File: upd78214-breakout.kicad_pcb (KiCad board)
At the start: 2 copper layers, 50 x 50 mm, 9 parts, among them U1 upd78214-64p-qfp, U2 tmp87c800df, X1 USB-B1HSB6

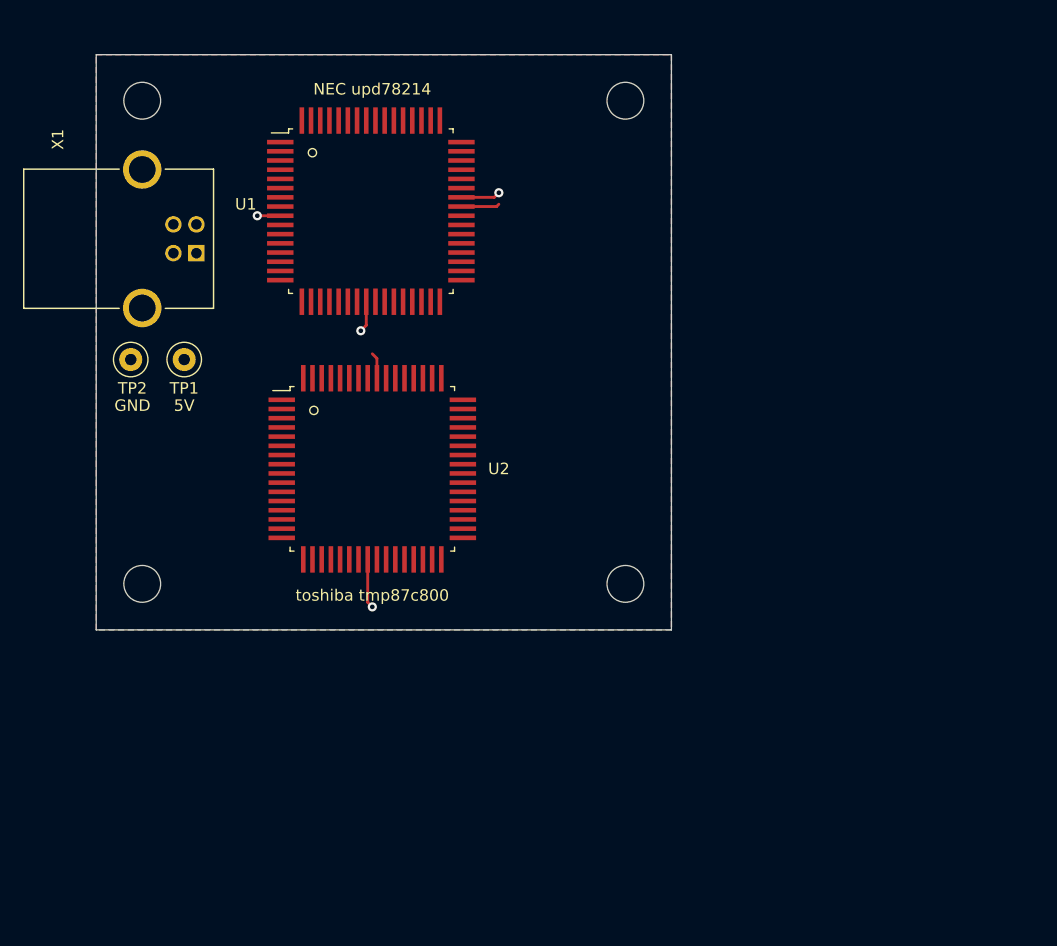
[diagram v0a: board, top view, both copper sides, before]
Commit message: Breakout pins for NEC
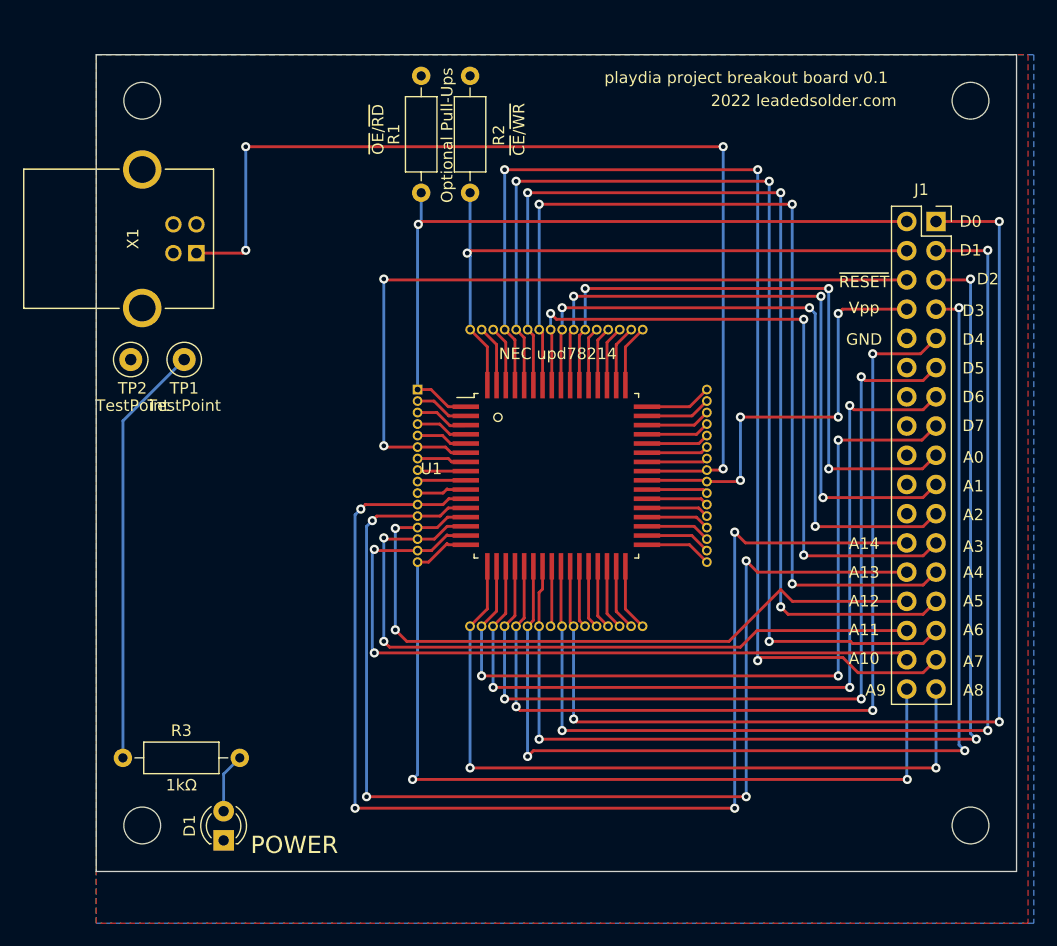
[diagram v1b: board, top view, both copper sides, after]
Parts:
- removed U2: tmp87c800df, NEC:QFP-64_14x14_Pitch0.8mm
- added D1: LED, LED_THT:LED_D3.0mm, F.Cu at (91.1, 147.3)
- added J1: Conn_02x17_Odd_Even, Connector_PinSocket_2.54mm:PinSocket_2x17_P2.54mm_Vertical, F.Cu at (153.0, 93.5)
- added R1: R_Small_US, Resistor_THT:R_Axial_DIN0207_L6.3mm_D2.5mm_P10.16mm_Horizontal, F.Cu at (108.2, 91.0)
- added R2: R_Small_US, Resistor_THT:R_Axial_DIN0207_L6.3mm_D2.5mm_P10.16mm_Horizontal, F.Cu at (112.5, 91.0)
- added R3: 1kΩ, Resistor_THT:R_Axial_DIN0207_L6.3mm_D2.5mm_P10.16mm_Horizontal, F.Cu at (82.3, 140.1)
- TP1: value 5V -> TestPoint
- TP2: value GND -> TestPoint
- moved REF** 69.8 mm to (156.0, 146.0)
- moved REF** 51.6 mm to (156.0, 83.0)
- moved U1 28.1 mm to (120.0, 115.6)
- moved REF** 21.0 mm to (84.0, 146.0)
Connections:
- U1 pad 1: unconnected-(U1-Pad1) -> /~{PROG_OE}
- U1 pad 11: unconnected-(U1-Pad11) -> /PROG_A14
- U1 pad 12: unconnected-(U1-Pad12) -> /PROG_A13
- U1 pad 13: unconnected-(U1-Pad13) -> /PROG_A12
- U1 pad 14: unconnected-(U1-Pad14) -> /PROG_A11
- U1 pad 15: unconnected-(U1-Pad15) -> /PROG_A10
- U1 pad 16: unconnected-(U1-Pad16) -> /PROG_A9
- U1 pad 17: unconnected-(U1-Pad17) -> /PROG_A8
- U1 pad 18: unconnected-(U1-Pad18) -> /PROG_D7
- U1 pad 19: unconnected-(U1-Pad19) -> /PROG_D6
- U1 pad 20: unconnected-(U1-Pad20) -> /PROG_D5
- U1 pad 21: unconnected-(U1-Pad21) -> /PROG_D4
- U1 pad 22: unconnected-(U1-Pad22) -> /PROG_D3
- U1 pad 23: unconnected-(U1-Pad23) -> /PROG_D2
- U1 pad 25: unconnected-(U1-Pad25) -> /PROG_D1
- U1 pad 26: unconnected-(U1-Pad26) -> /PROG_D0
- U1 pad 40: unconnected-(U1-Pad40) -> /PROG_Vpp
- U1 pad 54: unconnected-(U1-Pad54) -> /PROG_A0
- U1 pad 55: unconnected-(U1-Pad55) -> /PROG_A1
- U1 pad 56: unconnected-(U1-Pad56) -> /PROG_A2
- U1 pad 57: unconnected-(U1-Pad57) -> /PROG_A3
- U1 pad 58: unconnected-(U1-Pad58) -> /PROG_A4
- U1 pad 59: unconnected-(U1-Pad59) -> /PROG_A5
- U1 pad 6: unconnected-(U1-Pad6) -> /~{PROG_RESET}
- U1 pad 60: unconnected-(U1-Pad60) -> /PROG_A6
- U1 pad 61: unconnected-(U1-Pad61) -> /PROG_A7
- U1 pad 64: unconnected-(U1-Pad64) -> /~{PROG_CE}
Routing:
- net +5V: track 5.63 -> 126.4 mm, vias 0 -> 4
- net /PROG_A14: track 0.00 -> 108.1 mm, vias 0 -> 4
- net /PROG_A13: track 0.00 -> 100.7 mm, vias 0 -> 4
- net /PROG_A7: track 0.00 -> 100.4 mm, vias 0 -> 3
- net /PROG_D0: track 0.00 -> 99.5 mm, vias 0 -> 3
- net /PROG_D1: track 0.00 -> 97.6 mm, vias 0 -> 3
- net /PROG_D2: track 0.00 -> 96.4 mm, vias 0 -> 3
- net /PROG_D3: track 0.00 -> 95.7 mm, vias 0 -> 3
- net /PROG_A6: track 0.00 -> 95.1 mm, vias 0 -> 3
- net /PROG_A5: track 0.00 -> 89.2 mm, vias 0 -> 3
- net /PROG_A4: track 0.00 -> 83.9 mm, vias 0 -> 3
- net /PROG_D4: track 0.00 -> 80.7 mm, vias 0 -> 3
- net /PROG_D5: track 0.00 -> 78.0 mm, vias 0 -> 3
- net /PROG_A9: track 0.00 -> 74.8 mm, vias 0 -> 2
- net /PROG_D6: track 0.00 -> 74.6 mm, vias 0 -> 3
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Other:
- board size 50 x 50 mm -> 80 x 71 mm
- board text added: "A0"
- board text added: "A1"
- board text added: "A10"
- board text added: "A11"
- board text added: "A12"
- board text added: "A13"
- board text added: "A14"
- board text added: "A2"
- board text added: "A3"
- board text added: "A4"
- board text added: "A5"
- board text added: "A6"
- board text added: "A7"
- board text added: "A8"
- board text added: "A9"
- board text added: "D0"
- board text added: "D1"
- board text added: "D2"
- board text added: "D3"
- board text added: "D4"
- board text added: "D5"
- board text added: "D6"
- board text added: "D7"
- board text added: "GND"
- board text added: "Optional Pull-Ups"
- board text added: "POWER"
- board text added: "Vpp"
- board text added: "~{CE}/~{WR}"
- board text added: "~{OE}/~{RD}"
- board text added: "~{RESET}"
- board text removed: "toshiba tmp87c800"

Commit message: Dumper V1 sent to Jonko
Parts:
- added SPARE: DIP-14_W7.62mm_LongPads, Package_DIP:DIP-14_W7.62mm_LongPads, F.Cu at (88.4, 115.6)
- moved X1 6.81 mm to (90.8, 94.7)
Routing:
- net +5V: track 126.4 -> 71.5 mm, vias 4 -> 2
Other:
- board text added: "+5V"

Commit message: Break out NMI pin
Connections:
- J1 pad 22: unconnected-(J1-Pad22) -> /PROG_NMI
- U1 pad 28: unconnected-(U1-Pad28) -> /PROG_NMI
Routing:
- net /PROG_NMI: track 0.00 -> 51.8 mm, vias 0 -> 3
- net unconnected-(U1-Pad28): track 5.49 -> 0.00 mm
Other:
- board text added: "playdia project breakout board v0.2"
- board text removed: "playdia project breakout board v0.1"
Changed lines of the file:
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@@
   (net 24 "/PROG_A8")
   (net 25 "unconnected-(U1-Pad27)")
-  (net 26 "unconnected-(U1-Pad28)")
+  (net 26 "/PROG_NMI")
   (net 27 "unconnected-(U1-Pad29)")
   (net 28 "unconnected-(U1-Pad30)")
@@
   (net 68 "unconnected-(J1-Pad18)")
   (net 69 "unconnected-(J1-Pad20)")
-  (net 70 "unconnected-(J1-Pad22)")
-  (net 71 "Net-(D1-Pad2)")
+  (net 70 "Net-(D1-Pad2)")
   (footprint "TestPoint:TestPoint_Loop_D2.50mm_Drill1.0mm" (layer "F.Cu")
     (at 83 105.5)
@@
       (net 25 "unconnected-(U1-Pad27)") (pinfunction "ASTB") (pintype "output"))
     (pad "28" smd rect (at 2.8 7.874) (size 0.4 2.3) (layers "F.Cu" "F.Paste" "F.Mask")
-      (net 26 "unconnected-(U1-Pad28)") (pinfunction "p2,0/nmi") (pintype "input"))
+      (net 26 "/PROG_NMI") (pinfunction "p2,0/nmi") (pintype "input"))
     (pad "28" thru_hole oval (at 3.493 13.081 180) (size 0.85 0.85) (drill 0.5) (layers *.Cu *.Mask)
-      (net 26 "unconnected-(U1-Pad28)") (pinfunction "p2,0/nmi") (pintype "input"))
+      (net 26 "/PROG_NMI") (pinfunction "p2,0/nmi") (pintype "input"))
     (pad "29" thru_hole oval (at 4.493 13.081 90) (size 0.85 0.85) (drill 0.5) (layers *.Cu *.Mask)
       (net 27 "unconnected-(U1-Pad29)") (pinfunction "p2,1/intp0") (pintype "input"))
@@
       (net 57 "GND") (pinfunction "K") (pintype "passive"))
     (pad "2" thru_hole circle (at 2.54 0 90) (size 1.8 1.8) (drill 0.9) (layers *.Cu *.Mask)
-      (net 71 "Net-(D1-Pad2)") (pinfunction "A") (pintype "passive"))
+      (net 70 "Net-(D1-Pad2)") (pinfunction "A") (pintype "passive"))
     (model "${KICAD6_3DMODEL_DIR}/LED_THT.3dshapes/LED_D3.0mm.wrl"
       (offset (xyz 0 0 0))
@@
       (net 18 "/PROG_A2") (pinfunction "Pin_21") (pintype "passive"))
     (pad "22" thru_hole oval (at -2.54 25.4) (size 1.7 1.7) (drill 1) (layers *.Cu *.Mask)
-      (net 70 "unconnected-(J1-Pad22)") (pinfunction "Pin_22") (pintype "passive+no_connect"))
+      (net 26 "/PROG_NMI") (pinfunction "Pin_22") (pintype "passive"))
     (pad "23" thru_hole oval (at 0 27.94) (size 1.7 1.7) (drill 1) (layers *.Cu *.Mask)
       (net 19 "/PROG_A3") (pinfunction "Pin_23") (pintype "passive"))
@@
       (net 58 "+5V") (pintype "passive"))
     (pad "2" thru_hole oval (at 10.16 0) (size 1.6 1.6) (drill 0.8) (layers *.Cu *.Mask)
-      (net 71 "Net-(D1-Pad2)") (pintype "passive"))
+      (net 70 "Net-(D1-Pad2)") (pintype "passive"))
     (model "${KICAD6_3DMODEL_DIR}/Resistor_THT.3dshapes/R_Axial_DIN0207_L6.3mm_D2.5mm_P10.16mm_Horizontal.wrl"
       (offset (xyz 0 0 0))
@@
       (effects (font (size 1.001228 1.001228) (thickness 0.15)))
     )
+    (fp_line (start 6.05 2) (end 6.05 10.3) (layer "F.SilkS") (width 0.127))
+    (fp_line (start 6.05 -6.2) (end 6.05 -2) (layer "F.SilkS") (width 0.127))
+    (fp_line (start -6.05 -2) (end -6.05 -6.2) (layer "F.SilkS") (width 0.127))
+    (fp_line (start -6.05 10.3) (end -6.05 2) (layer "F.SilkS") (width 0.127))
     (fp_line (start -6.05 -6.2) (end 6.05 -6.2) (layer "F.SilkS") (width 0.127))
-    (fp_line (start -6.05 -2) (end -6.05 -6.2) (layer "F.SilkS") (width 0.127))
-    (fp_line (start 6.05 -6.2) (end 6.05 -2) (layer "F.SilkS") (width 0.127))
-    (fp_line (start 6.05 2) (end 6.05 10.3) (layer "F.SilkS") (width 0.127))
-    (fp_line (start -6.05 10.3) (end -6.05 2) (layer "F.SilkS") (width 0.127))
     (fp_line (start 6.05 10.3) (end -6.05 10.3) (layer "F.SilkS") (width 0.127))
+    (fp_line (start -8 -6.5) (end 8 -6.5) (layer "F.CrtYd") (width 0.05))
     (fp_line (start 8 10.5) (end -8 10.5) (layer "F.CrtYd") (width 0.05))
+    (fp_line (start 8 -6.5) (end 8 10.5) (layer "F.CrtYd") (width 0.05))
     (fp_line (start -8 10.5) (end -8 -6.5) (layer "F.CrtYd") (width 0.05))
-    (fp_line (start -8 -6.5) (end 8 -6.5) (layer "F.CrtYd") (width 0.05))
-    (fp_line (start 8 -6.5) (end 8 10.5) (layer "F.CrtYd") (width 0.05))
     (pad "1" thru_hole rect (at 1.25 -4.71 270) (size 1.428 1.428) (drill 0.92) (layers *.Cu *.Mask)
       (net 58 "+5V") (pinfunction "VCC") (pintype "power_out"))
@@
     (effects (font (size 1 1) (thickness 0.15)))
   )
-  (gr_text "playdia project breakout board v0.1" (at 136.5 81) (layer "F.SilkS")
+  (gr_text "playdia project breakout board v0.2" (at 136.5 81) (layer "F.SilkS")
     (effects (font (size 1 1) (thickness 0.15)))
   )
@@
   (segment (start 115.493 134.993) (end 115.493 128.681) (width 0.25) (layer "B.Cu") (net 13))
   (segment (start 114.493 128.681) (end 115.6 127.574) (width 0.25) (layer "F.Cu") (net 14))
+  (segment (start 114.651501 134.151501) (end 114.5 134) (width 0.25) (layer "F.Cu") (net 14))
   (segment (start 151.875489 109.864511) (end 145.864511 109.864511) (width 0.25) (layer "F.Cu") (net 14))
   (segment (start 153 108.74) (end 151.875489 109.864511) (width 0.25) (layer "F.Cu") (net 14))
   (segment (start 145.864511 109.864511) (end 145.5 109.5) (width 0.25) (layer "F.Cu") (net 14))
   (segment (start 115.6 127.574) (end 115.6 123.474) (width 0.25) (layer "F.Cu") (net 14))
-  (segment (start 145.5 134) (end 114.5 134) (width 0.25) (layer "F.Cu") (net 14))
+  (segment (start 145.5 134) (end 145.348499 134.151501) (width 0.25) (layer "F.Cu") (net 14))
+  (segment (start 145.348499 134.151501) (end 114.651501 134.151501) (width 0.25) (layer "F.Cu") (net 14))
   (via (at 114.5 134) (size 0.8) (drill 0.4) (layers "F.Cu" "B.Cu") (net 14))
   (via (at 145.5 134) (size 0.8) (drill 0.4) (layers "F.Cu" "B.Cu") (net 14))
@@
   (segment (start 151.78 112.5) (end 144.5 112.5) (width 0.25) (layer "F.Cu") (net 15))
   (segment (start 114.8 127.374) (end 114.8 123.474) (width 0.25) (layer "F.Cu") (net 15))
+  (segment (start 144.5 133) (end 144.302499 132.802499) (width 0.25) (layer "F.Cu") (net 15))
+  (segment (start 113.697501 132.802499) (end 113.5 133) (width 0.25) (layer "F.Cu") (net 15))
   (segment (start 113.493 128.681) (end 114.8 127.374) (width 0.25) (layer "F.Cu") (net 15))
-  (segment (start 144.5 133) (end 113.5 133) (width 0.25) (layer "F.Cu") (net 15))
   (segment (start 153 111.28) (end 151.78 112.5) (width 0.25) (layer "F.Cu") (net 15))
+  (segment (start 144.302499 132.802499) (end 113.697501 132.802499) (width 0.25) (layer "F.Cu") (net 15))
   (via (at 144.5 133) (size 0.8) (drill 0.4) (layers "F.Cu" "B.Cu") (net 15))
   (via (at 144.5 112.5) (size 0.8) (drill 0.4) (layers "F.Cu" "B.Cu") (net 15))
@@
   (segment (start 122 123.474) (end 122 128.188) (width 0.25) (layer "F.Cu") (net 25))
   (segment (start 122.8 127.988) (end 123.493 128.681) (width 0.25) (layer "F.Cu") (net 26))
+  (segment (start 143.411 118.9) (end 150.46 118.9) (width 0.25) (layer "F.Cu") (net 26))
+  (segment (start 123.571 133.477) (end 143.383 133.477) (width 0.25) (layer "F.Cu") (net 26))
+  (segment (start 143.383 118.872) (end 143.411 118.9) (width 0.25) (layer "F.Cu") (net 26))
   (segment (start 122.8 123.474) (end 122.8 127.988) (width 0.25) (layer "F.Cu") (net 26))
+  (via (at 123.571 133.477) (size 0.8) (drill 0.4) (layers "F.Cu" "B.Cu") (net 26))
+  (via (at 143.383 133.477) (size 0.8) (drill 0.4) (layers "F.Cu" "B.Cu") (net 26))
+  (via (at 143.383 118.872) (size 0.8) (drill 0.4) (layers "F.Cu" "B.Cu") (net 26))
+  (segment (start 123.493 133.399) (end 123.571 133.477) (width 0.25) (layer "B.Cu") (net 26))
+  (segment (start 123.493 128.681) (end 123.493 133.399) (width 0.25) (layer "B.Cu") (net 26))
+  (segment (start 143.383 133.477) (end 143.383 118.872) (width 0.25) (layer "B.Cu") (net 26))
   (segment (start 123.6 123.474) (end 123.6 127.788) (width 0.25) (layer "F.Cu") (net 27))
   (segment (start 123.6 127.788) (end 124.493 128.681) (width 0.25) (layer "F.Cu") (net 27))
@@
   (segment (start 108 93.75) (end 107.935 93.815) (width 0.25) (layer "B.Cu") (net 64))
   (segment (start 108.25 93.5) (end 108.25 91) (width 0.25) (layer "B.Cu") (net 64))
-  (segment (start 91.075 141.53) (end 92.48 140.125) (width 0.25) (layer "B.Cu") (net 71))
-  (segment (start 91.075 144.76) (end 91.075 141.53) (width 0.25) (layer "B.Cu") (net 71))
+  (segment (start 91.075 141.53) (end 92.48 140.125) (width 0.25) (layer "B.Cu") (net 70))
+  (segment (start 91.075 144.76) (end 91.075 141.53) (width 0.25) (layer "B.Cu") (net 70))
   (zone (net 58) (net_name "+5V") (layer "F.Cu") (hatch edge 0.508)
     (connect_pads (clearance 0.508))

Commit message: Re-route complete
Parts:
- added R10: 10kΩ, Resistor_THT:R_Axial_DIN0207_L6.3mm_D2.5mm_P10.16mm_Horizontal, F.Cu at (123.8, 136.5)
- added R11: 10kΩ, Resistor_THT:R_Axial_DIN0207_L6.3mm_D2.5mm_P10.16mm_Horizontal, F.Cu at (120.7, 136.5)
- added R12: 10kΩ, Resistor_THT:R_Axial_DIN0207_L6.3mm_D2.5mm_P10.16mm_Horizontal, F.Cu at (117.5, 136.5)
- added R13: 10kΩ, Resistor_THT:R_Axial_DIN0207_L6.3mm_D2.5mm_P10.16mm_Horizontal, F.Cu at (114.3, 136.5)
- added R14: 10kΩ, Resistor_THT:R_Axial_DIN0207_L6.3mm_D2.5mm_P10.16mm_Horizontal, F.Cu at (131.6, 90.9)
- added R15: 10kΩ, Resistor_THT:R_Axial_DIN0207_L6.3mm_D2.5mm_P10.16mm_Horizontal, F.Cu at (111.1, 136.5)
- added R16: 10kΩ, Resistor_THT:R_Axial_DIN0207_L6.3mm_D2.5mm_P10.16mm_Horizontal, F.Cu at (122.4, 90.9)
- added R17: 10kΩ, Resistor_THT:R_Axial_DIN0207_L6.3mm_D2.5mm_P10.16mm_Horizontal, F.Cu at (128.5, 90.9)
- added R18: 10kΩ, Resistor_THT:R_Axial_DIN0207_L6.3mm_D2.5mm_P10.16mm_Horizontal, F.Cu at (108.0, 136.5)
- added R19: 10kΩ, Resistor_THT:R_Axial_DIN0207_L6.3mm_D2.5mm_P10.16mm_Horizontal, F.Cu at (125.5, 90.9)
- added R20: 10kΩ, Resistor_THT:R_Axial_DIN0207_L6.3mm_D2.5mm_P10.16mm_Horizontal, F.Cu at (127.0, 136.5)
- added R4: 10kΩ, Resistor_THT:R_Axial_DIN0207_L6.3mm_D2.5mm_P10.16mm_Horizontal, F.Cu at (137.7, 80.8)
- added R5: 10kΩ, Resistor_THT:R_Axial_DIN0207_L6.3mm_D2.5mm_P10.16mm_Horizontal, F.Cu at (134.6, 90.9)
- added R6: 10kΩ, Resistor_THT:R_Axial_DIN0207_L6.3mm_D2.5mm_P10.16mm_Horizontal, F.Cu at (104.8, 136.5)
- added R7: 10kΩ, Resistor_THT:R_Axial_DIN0207_L6.3mm_D2.5mm_P10.16mm_Horizontal, F.Cu at (140.7, 90.9)
- added R8: 10kΩ, Resistor_THT:R_Axial_DIN0207_L6.3mm_D2.5mm_P10.16mm_Horizontal, F.Cu at (119.4, 90.9)
- added R9: 10kΩ, Resistor_THT:R_Axial_DIN0207_L6.3mm_D2.5mm_P10.16mm_Horizontal, F.Cu at (143.8, 90.9)
- moved R3 18.3 mm to (83.8, 121.9), turned to -90 degrees
- moved D1 7.51 mm to (88.3, 140.3), turned to 180 degrees
- turned U1 to 90 degrees
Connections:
- J1 pad 20: unconnected-(J1-Pad20) -> /PROG_NMI
- J1 pad 22: /PROG_NMI -> /PROG_A15
- U1 pad 10: unconnected-(U1-Pad10) -> /PROG_A15
- U1 pad 16: /PROG_A9 -> Net-(U1-Pad16)
- U1 pad 2: unconnected-(U1-Pad2) -> Net-(U1-Pad2)
- U1 pad 29: unconnected-(U1-Pad29) -> /PROG_A9
- U1 pad 3: unconnected-(U1-Pad3) -> Net-(U1-Pad3)
- U1 pad 30: unconnected-(U1-Pad30) -> GND
- U1 pad 31: unconnected-(U1-Pad31) -> GND
- U1 pad 32: unconnected-(U1-Pad32) -> GND
- U1 pad 33: unconnected-(U1-Pad33) -> GND
- U1 pad 34: unconnected-(U1-Pad34) -> GND
- U1 pad 35: unconnected-(U1-Pad35) -> GND
- U1 pad 38: unconnected-(U1-Pad38) -> Net-(U1-Pad38)
- U1 pad 39: unconnected-(U1-Pad39) -> Net-(U1-Pad39)
- U1 pad 4: unconnected-(U1-Pad4) -> Net-(U1-Pad4)
- U1 pad 42: GND -> Net-(U1-Pad42)
- U1 pad 43: unconnected-(U1-Pad43) -> Net-(U1-Pad43)
- U1 pad 44: unconnected-(U1-Pad44) -> Net-(U1-Pad44)
- U1 pad 45: unconnected-(U1-Pad45) -> Net-(U1-Pad45)
- U1 pad 46: unconnected-(U1-Pad46) -> Net-(U1-Pad46)
- U1 pad 47: unconnected-(U1-Pad47) -> Net-(U1-Pad47)
- U1 pad 48: unconnected-(U1-Pad48) -> Net-(U1-Pad48)
- U1 pad 49: unconnected-(U1-Pad49) -> Net-(U1-Pad49)
- U1 pad 5: unconnected-(U1-Pad5) -> Net-(U1-Pad5)
- U1 pad 62: unconnected-(U1-Pad62) -> Net-(U1-Pad62)
- U1 pad 63: unconnected-(U1-Pad63) -> Net-(U1-Pad63)
- U1 pad 8: unconnected-(U1-Pad8) -> GND
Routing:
- net /PROG_A2: track 58.5 -> 154.9 mm, vias 3 -> 6
- net /PROG_A14: track 108.1 -> 34.9 mm, vias 4 -> 1
- net /PROG_A1: track 57.2 -> 129.2 mm, vias 3 -> 6
- net /PROG_A3: track 61.0 -> 129.4 mm, vias 3 -> 6
- net /PROG_A15: track 0.00 -> 67.7 mm, vias 0 -> 3
- net /PROG_A13: track 100.7 -> 33.0 mm, vias 4 -> 1
- net +5V: track 71.5 -> 5.25 mm, vias 2 -> 0
- net GND: track 14.8 -> 71.6 mm
- net /PROG_D0: track 99.5 -> 44.6 mm, vias 3 -> 2
- net /PROG_D3: track 95.7 -> 41.3 mm, vias 3 -> 2
- net /PROG_D2: track 96.4 -> 42.6 mm, vias 3 -> 2
- net /PROG_D1: track 97.6 -> 43.9 mm, vias 3 -> 2
- net /PROG_A0: track 55.6 -> 108.1 mm, vias 3 -> 4
- net Net-(U1-Pad38): track 0.00 -> 52.2 mm, vias 0 -> 2
- net Net-(U1-Pad42): track 0.00 -> 47.1 mm, vias 0 -> 2
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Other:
- board text added: "1"
- board text added: "10kΩ"
- board text added: "16"
- board text added: "17"
- board text added: "32"
- board text added: "33"
- board text added: "48"
- board text added: "49"
- board text added: "64"
- board text added: "A15"
- board text added: "NMI"
- board text added: "~{CE}"
- board text added: "~{OE}"
